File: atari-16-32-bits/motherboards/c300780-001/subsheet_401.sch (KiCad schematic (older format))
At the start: 1 part, among them U401 STE_GSTSHIFTER_PHY

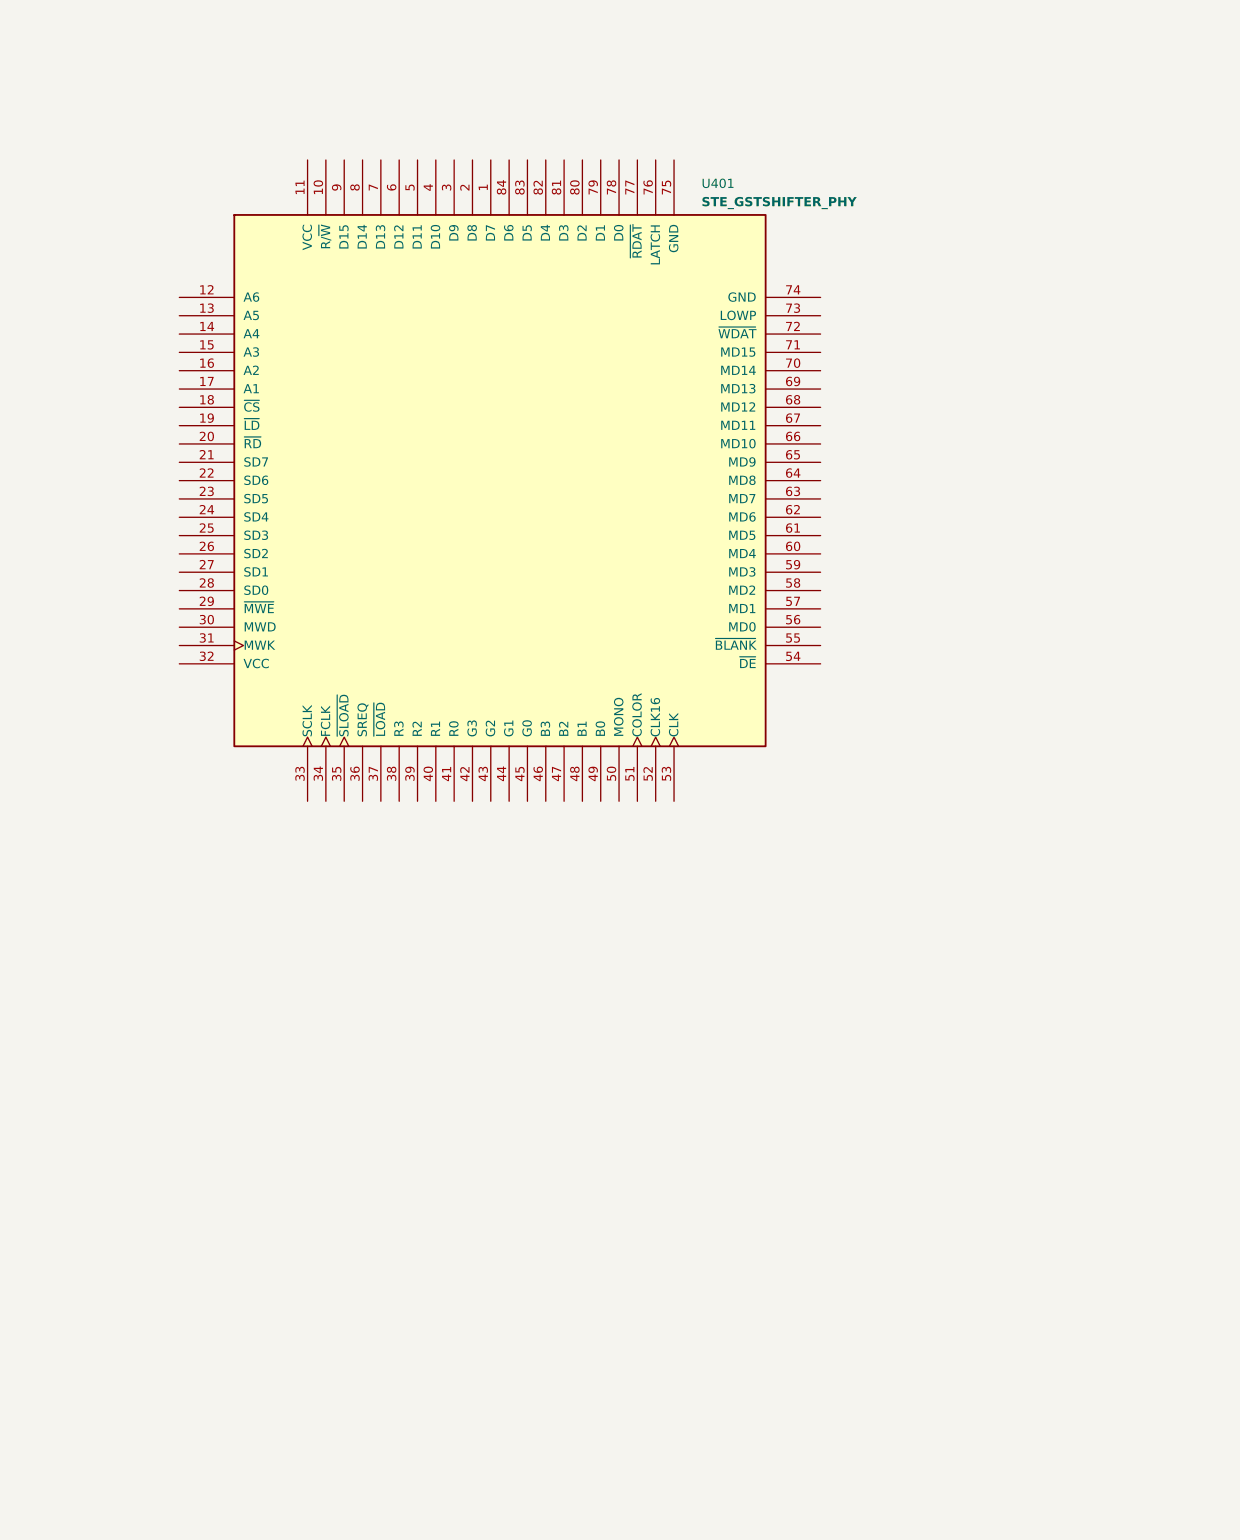
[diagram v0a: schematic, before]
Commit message: done subsheet 401 : the shifter
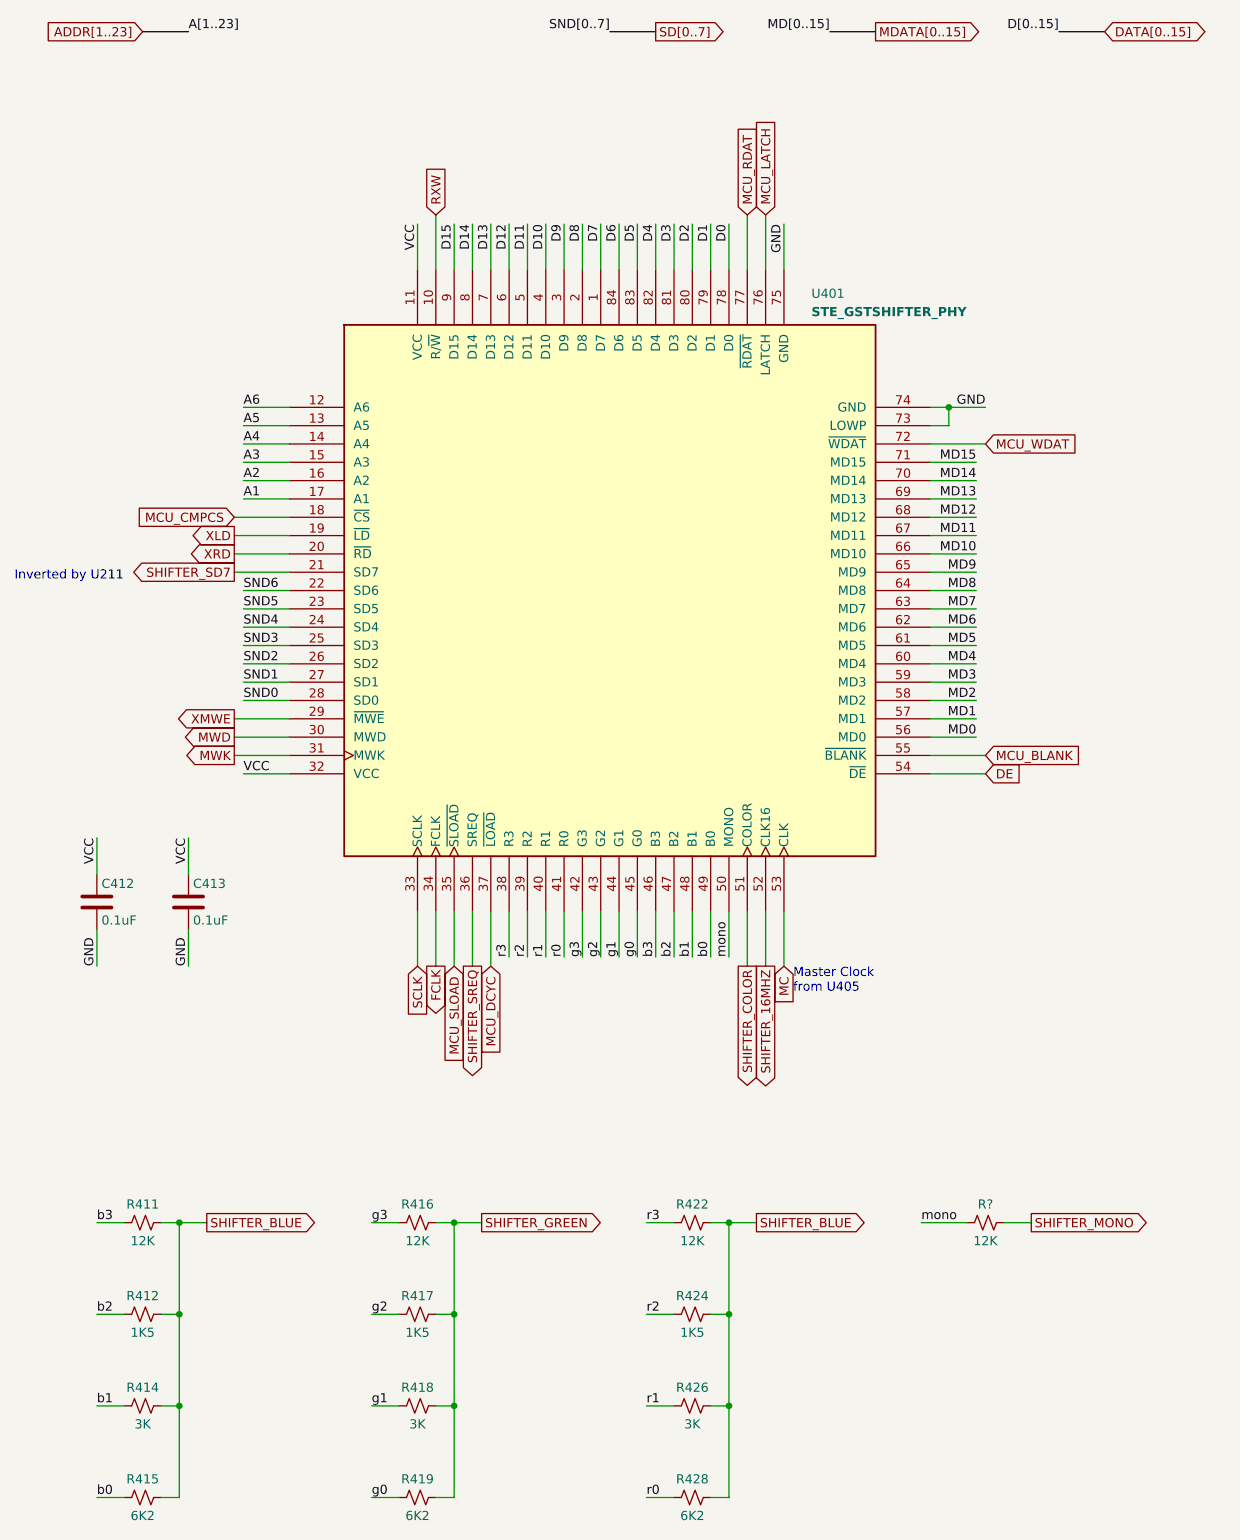
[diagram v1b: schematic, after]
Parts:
- added C412, C413: 0.1uF, symbol Device:C
- added R411, R416, R422, R?: 12K, symbol Device:R_Small_US
- added R412, R417, R424: 1K5, symbol Device:R_Small_US
- added R414, R418, R426: 3K, symbol Device:R_Small_US
- added R415, R419, R428: 6K2, symbol Device:R_Small_US
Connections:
- net D7: now reaches U401.1 (D7)
- net RXW: now reaches U401.10 (R/~W~)
- net VCC: now reaches U401.11 (VCC)
- net VCC: now also U401.32 (VCC), C412.1, C413.1
- net A6: now reaches U401.12 (A6)
- net A5: now reaches U401.13 (A5)
- net A4: now reaches U401.14 (A4)
- net A3: now reaches U401.15 (A3)
- net A2: now reaches U401.16 (A2)
- net A1: now reaches U401.17 (A1)
- net MCU_CMPCS: now reaches U401.18 (~CS~)
- net XLD: now reaches U401.19 (~LD~)
- net D8: now reaches U401.2 (D8)
- net XRD: now reaches U401.20 (~RD~)
- net SHIFTER_SD7: now reaches U401.21 (SD7)
- net SND6: now reaches U401.22 (SD6)
- net SND5: now reaches U401.23 (SD5)
- net SND4: now reaches U401.24 (SD4)
- net SND3: now reaches U401.25 (SD3)
- net SND2: now reaches U401.26 (SD2)
- net SND1: now reaches U401.27 (SD1)
- net SND0: now reaches U401.28 (SD0)
- net XMWE: now reaches U401.29 (~MWE~)
- net D9: now reaches U401.3 (D9)
- net MWD: now reaches U401.30 (MWD)
- net MWK: now reaches U401.31 (MWK)
- net SCLK: now reaches U401.33 (SCLK)
- net FCLK: now reaches U401.34 (FCLK)
- net MCU_SLOAD: now reaches U401.35 (~SLOAD~)
- net SHIFTER_SREQ: now reaches U401.36 (SREQ)
- net MCU_DCYC: now reaches U401.37 (~LOAD~)
- net r3: now reaches U401.38 (R3)
- net r3: now also R422.2
- net r2: now reaches U401.39 (R2)
- net r2: now also R424.2
- net D10: now reaches U401.4 (D10)
- net r1: now reaches U401.40 (R1)
- net r1: now also R426.2
- net r0: now reaches U401.41 (R0)
- net r0: now also R428.2
- net g3: now reaches U401.42 (G3)
- net g3: now also R416.2
- net g2: now reaches U401.43 (G2)
- net g2: now also R417.2
- net g1: now reaches U401.44 (G1)
- net g1: now also R418.2
- net g0: now reaches U401.45 (G0)
- net g0: now also R419.2
- net b3: now reaches U401.46 (B3)
- net b3: now also R411.2
- net b2: now reaches U401.47 (B2)
- net b2: now also R412.2
- net b1: now reaches U401.48 (B1)
- net b1: now also R414.2
- net b0: now reaches U401.49 (B0)
- net b0: now also R415.2
- net D11: now reaches U401.5 (D11)
- net mono: now reaches U401.50 (MONO)
- net mono: now also R?.2
- net SHIFTER_COLOR: now reaches U401.51 (COLOR)
- net SHIFTER_16MHZ: now reaches U401.52 (CLK16)
- net MC: now reaches U401.53 (CLK)
- net DE: now reaches U401.54 (~DE~)
- net MCU_BLANK: now reaches U401.55 (~BLANK~)
- net MD0: now reaches U401.56 (MD0)
- net MD1: now reaches U401.57 (MD1)
- net MD2: now reaches U401.58 (MD2)
- net MD3: now reaches U401.59 (MD3)
- net D12: now reaches U401.6 (D12)
- net MD4: now reaches U401.60 (MD4)
- net MD5: now reaches U401.61 (MD5)
- net MD6: now reaches U401.62 (MD6)
- net MD7: now reaches U401.63 (MD7)
- net MD8: now reaches U401.64 (MD8)
- net MD9: now reaches U401.65 (MD9)
- net MD10: now reaches U401.66 (MD10)
- net MD11: now reaches U401.67 (MD11)
- net MD12: now reaches U401.68 (MD12)
- net MD13: now reaches U401.69 (MD13)
- net D13: now reaches U401.7 (D13)
- net MD14: now reaches U401.70 (MD14)
- net MD15: now reaches U401.71 (MD15)
- net MCU_WDAT: now reaches U401.72 (~WDAT~)
- net GND: now reaches U401.73 (LOWP)
- net GND: now also U401.74 (GND), U401.75 (GND), C412.2, C413.2
- net MCU_LATCH: now reaches U401.76 (LATCH)
- net MCU_RDAT: now reaches U401.77 (~RDAT~)
- net D0: now reaches U401.78 (D0)
- net D1: now reaches U401.79 (D1)
- net D14: now reaches U401.8 (D14)
- net D2: now reaches U401.80 (D2)
- net D3: now reaches U401.81 (D3)
- net D4: now reaches U401.82 (D4)
- net D5: now reaches U401.83 (D5)
- net D6: now reaches U401.84 (D6)
- net D15: now reaches U401.9 (D15)
- new net SHIFTER_BLUE: R411.1, R412.1, R414.1, R415.1, R422.1, R424.1, R426.1, R428.1
- new net SHIFTER_GREEN: R416.1, R417.1, R418.1, R419.1
- new net SHIFTER_MONO: R?.1
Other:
- note added: "Inverted by U211"
- note added: "Master Clock\nfrom U405"
- moved on the sheet: U401

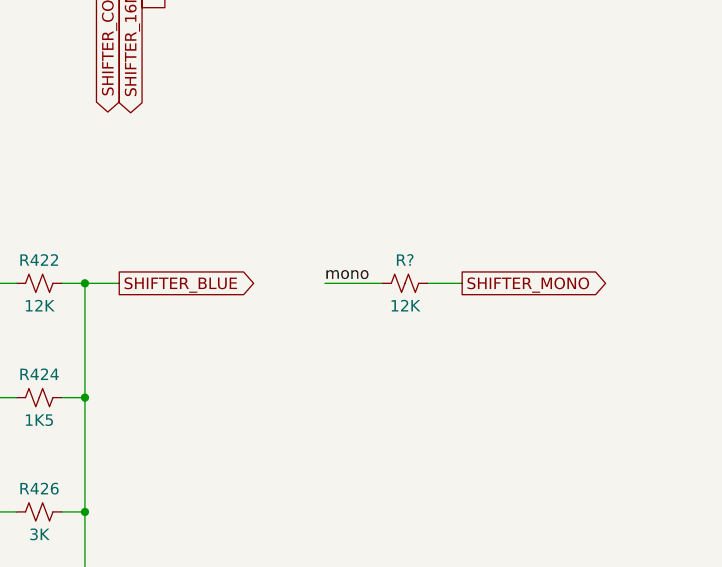
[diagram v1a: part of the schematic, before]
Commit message: fixed typo in subsheet 401 : R430
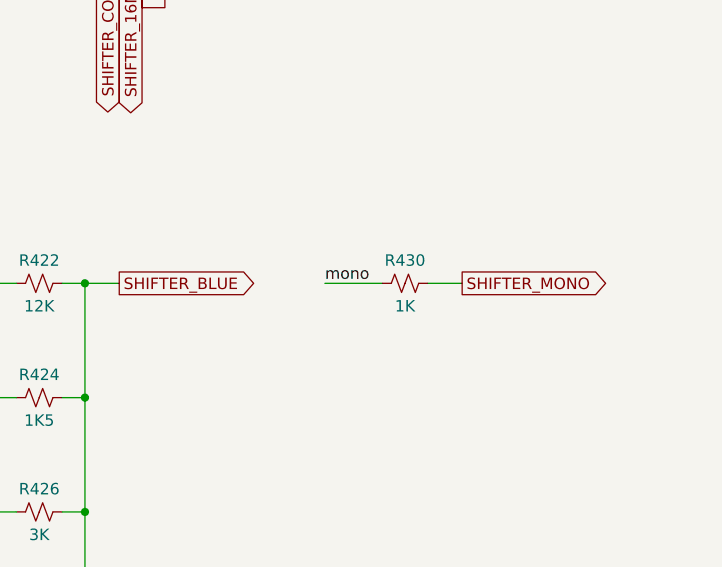
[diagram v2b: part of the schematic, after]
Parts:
- R430: renamed from R?; value 12K -> 1K
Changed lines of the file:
@@
 AR Path="/60AD8617/60BDFD77" Ref="R?"  Part="1"
 AR Path="/60AD332C/60BDFD77" Ref="R?"  Part="1"
-AR Path="/60AD33B6/60BDFD77" Ref="R?"  Part="1"
-F 0 "R?" V 6000 7500 50  0000 C CNN
-F 1 "12K" V 6200 7500 50  0000 C CNN
+AR Path="/60AD33B6/60BDFD77" Ref="R430"  Part="1"
+F 0 "R430" V 6000 7500 50  0000 C CNN
+F 1 "1K" V 6200 7500 50  0000 C CNN
 F 2 "" H 6100 7500 50  0001 C CNN
 F 3 "~" H 6100 7500 50  0001 C CNN

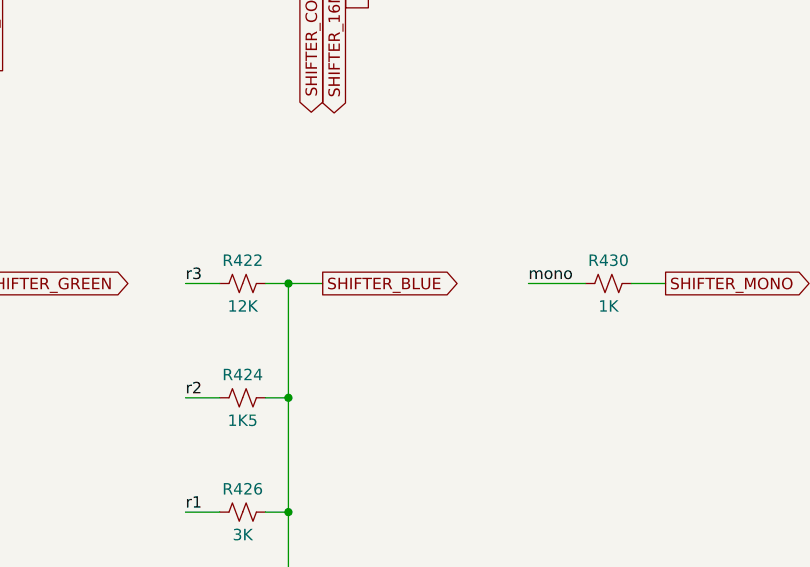
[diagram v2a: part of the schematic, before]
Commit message: wip subsheet 402 : genlock circuitry , remaining R and L annotations
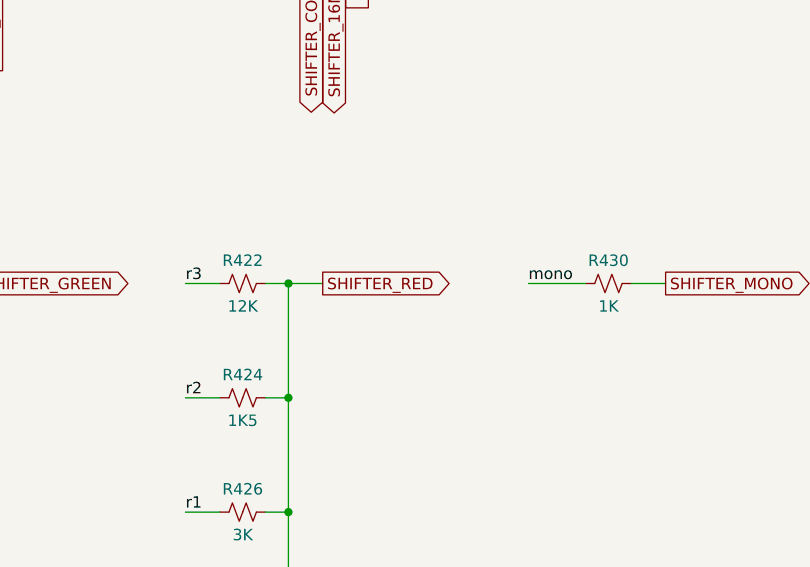
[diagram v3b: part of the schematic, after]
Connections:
- net SHIFTER_BLUE: no longer R422.1, R424.1, R426.1, R428.1
- new net SHIFTER_RED: R422.1, R424.1, R426.1, R428.1
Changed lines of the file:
@@
 $Descr A4 8268 11693 portrait
 encoding utf-8
-Sheet 20 20
+Sheet 20 21
 Title ""
 Date ""
@@
 SHIFTER_GREEN
 Text GLabel 4850 7500 2    50   Output ~ 0
-SHIFTER_BLUE
-$Comp
-L Device:R_Small_US R?
+SHIFTER_RED
+$Comp
+L Device:R_Small_US R?
